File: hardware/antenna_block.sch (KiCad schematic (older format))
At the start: 33 parts, among them P301 BNC

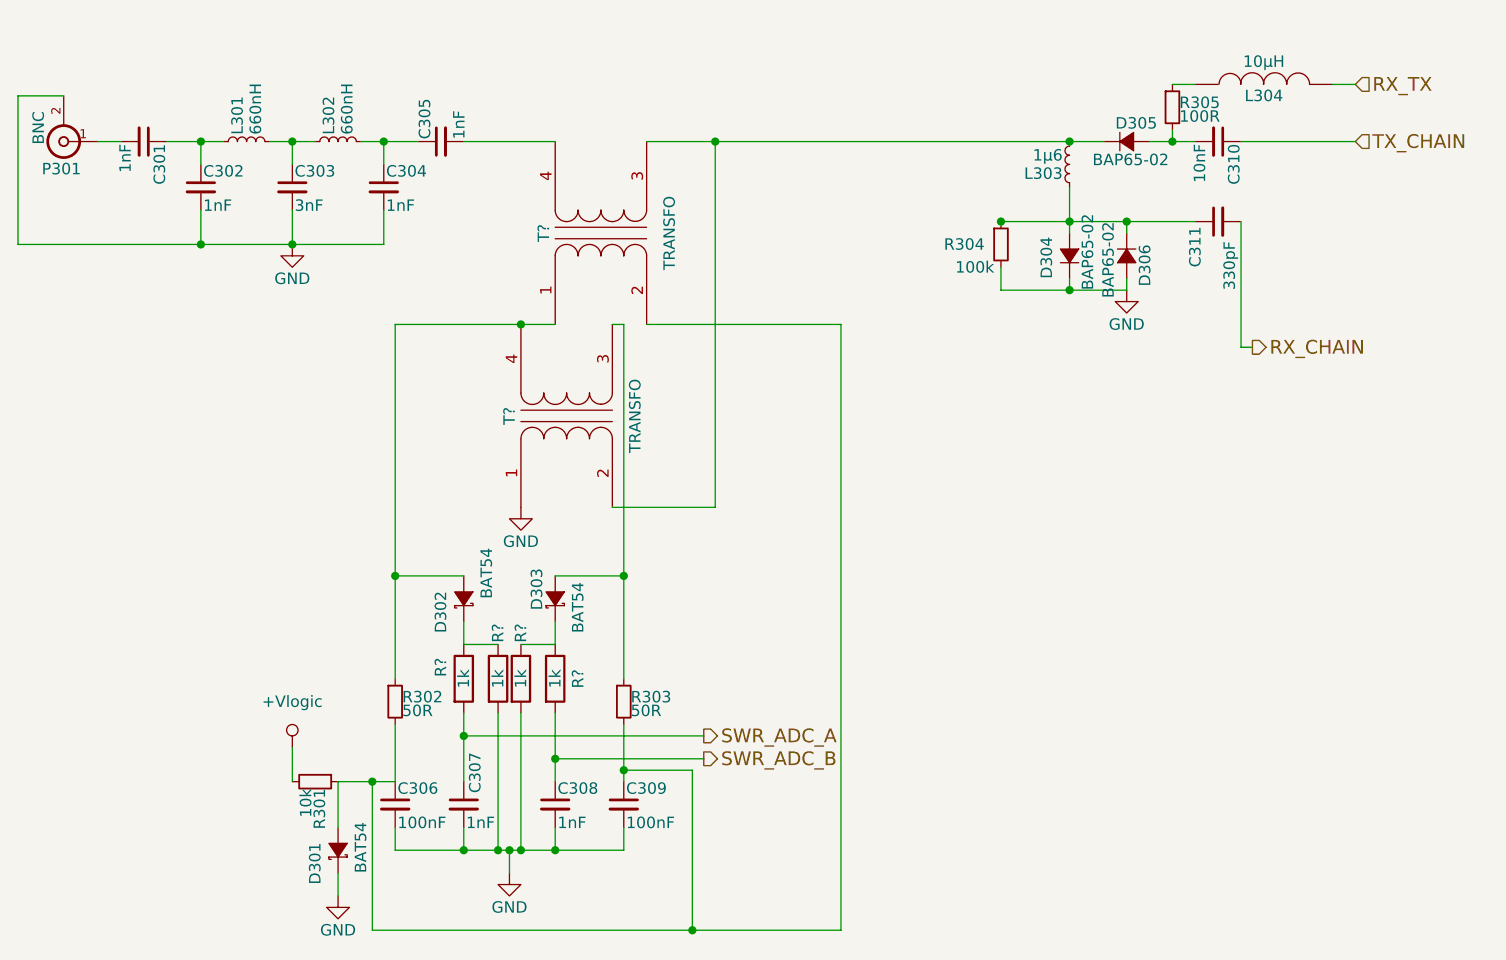
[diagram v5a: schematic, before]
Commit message: Fixed some bugs and annotated rest of the footprints
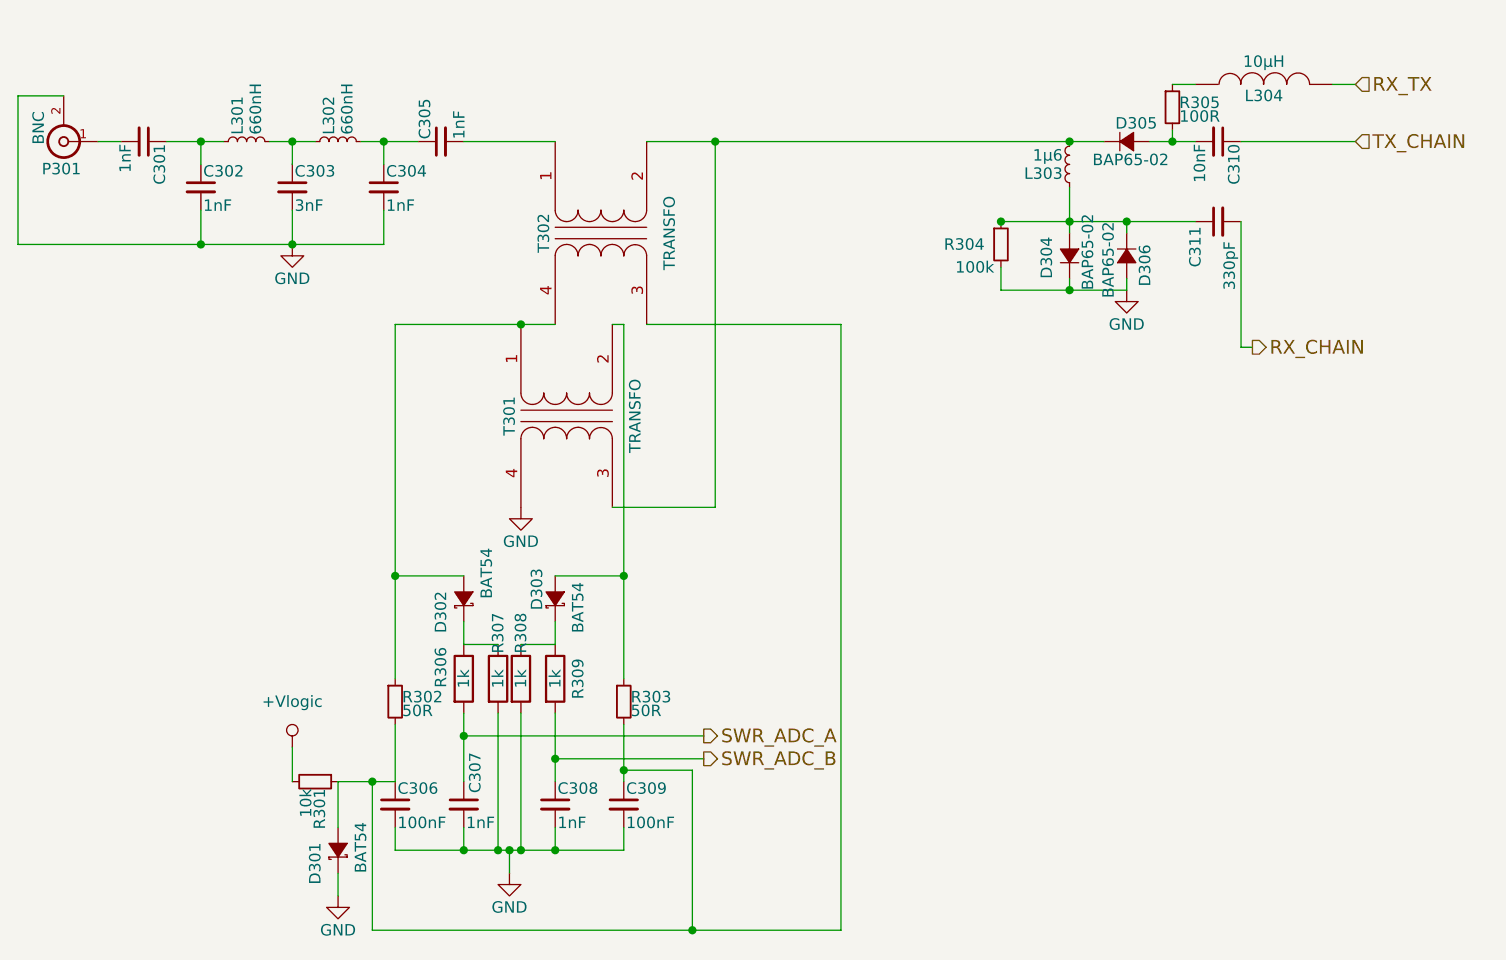
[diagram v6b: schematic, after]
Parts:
- C301, C302, C303, C304, C305, C306, C307, C308, C309, C310, C311: footprint Capacitors_SMD:C_0805 -> Capacitors_SMD:C_0805_HandSoldering
- D304, D305, D306: footprint (none) -> Diodes_SMD:SOD-523
- L301, L302, L303: footprint (none) -> Air_Coils_SML_NEOSID:Neosid_Air-Coil_SML_5turn_HDM0531A
- L304: footprint (none) -> Resistors_SMD:R_0805_HandSoldering
- P301: footprint (none) -> dodekaedri:BNC_right_angle
- R306, R307, R308, R309: renamed from R?; footprint (none) -> Resistors_SMD:R_0805_HandSoldering
- T301, T302: renamed from T?; footprint (none) -> dodekaedri:TRANSF_pads
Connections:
- net GND: now also T301.4 (SB); no longer T301.1 (AA)
- net at C305.2: now also T302.1 (AA); no longer T302.4 (SB)
- net at D302.2 (A), R302.1: now also T301.1 (AA), T302.4 (SB); no longer T301.4 (SB), T302.1 (AA)
- net at C306.1, C309.1, D301.2 (A)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: now also T302.3 (SA); no longer T302.2 (AB)
- net at D303.2 (A), R303.1: now also T301.2 (AB); no longer T301.3 (SA)
- net at D305.1 (K), L303.2: now also T301.3 (SA), T302.2 (AB); no longer T301.2 (AB), T302.3 (SA)
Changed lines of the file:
@@
 F 0 "P301" H 2810 3220 50  0000 C CNN
 F 1 "BNC" V 2910 3040 50  0000 C CNN
-F 2 "" H 2800 3100 50  0001 C CNN
+F 2 "dodekaedri:BNC_right_angle" H 2800 3100 50  0001 C CNN
 F 3 "" H 2800 3100 50  0000 C CNN
 	1    2800 3100
@@
 F 0 "C301" H 3160 3170 50  0000 L CNN
 F 1 "1nF" H 3160 3020 50  0000 L CNN
-F 2 "Capacitors_SMD:C_0805" H 3150 3100 50  0001 C CNN
+F 2 "Capacitors_SMD:C_0805_HandSoldering" H 3150 3100 50  0001 C CNN
 F 3 "" H 3150 3100 50  0000 C CNN
 	1    3150 3100
@@
 F 0 "C302" H 3410 3370 50  0000 L CNN
 F 1 "1nF" H 3410 3220 50  0000 L CNN
-F 2 "Capacitors_SMD:C_0805" H 3400 3300 50  0001 C CNN
+F 2 "Capacitors_SMD:C_0805_HandSoldering" H 3400 3300 50  0001 C CNN
 F 3 "" H 3400 3300 50  0000 C CNN
 	1    3400 3300
@@
 $EndComp
 $Comp
-L GND #PWR301
+L GND #PWR012
 U 1 1 57E329F5
 P 3800 3550
-F 0 "#PWR301" H 3800 3300 50  0001 C CNN
+F 0 "#PWR012" H 3800 3300 50  0001 C CNN
 F 1 "GND" H 3800 3400 50  0000 C CNN
 F 2 "" H 3800 3550 50  0000 C CNN
@@
 F 0 "L301" H 3630 3140 50  0000 L CNN
 F 1 "660nH" H 3630 3060 50  0000 L CNN
-F 2 "" H 3600 3100 50  0001 C CNN
+F 2 "Air_Coils_SML_NEOSID:Neosid_Air-Coil_SML_5turn_HDM0531A" H 3600 3100 50  0001 C CNN
 F 3 "" H 3600 3100 50  0000 C CNN
 	1    3600 3100
@@
 F 0 "L302" H 4030 3140 50  0000 L CNN
 F 1 "660nH" H 4030 3060 50  0000 L CNN
-F 2 "" H 4000 3100 50  0001 C CNN
+F 2 "Air_Coils_SML_NEOSID:Neosid_Air-Coil_SML_5turn_HDM0531A" H 4000 3100 50  0001 C CNN
 F 3 "" H 4000 3100 50  0000 C CNN
 	1    4000 3100
@@
 F 0 "C303" H 3810 3370 50  0000 L CNN
 F 1 "3nF" H 3810 3220 50  0000 L CNN
-F 2 "Capacitors_SMD:C_0805" H 3800 3300 50  0001 C CNN
+F 2 "Capacitors_SMD:C_0805_HandSoldering" H 3800 3300 50  0001 C CNN
 F 3 "" H 3800 3300 50  0000 C CNN
 	1    3800 3300
@@
 F 0 "C304" H 4210 3370 50  0000 L CNN
 F 1 "1nF" H 4210 3220 50  0000 L CNN
-F 2 "Capacitors_SMD:C_0805" H 4200 3300 50  0001 C CNN
+F 2 "Capacitors_SMD:C_0805_HandSoldering" H 4200 3300 50  0001 C CNN
 F 3 "" H 4200 3300 50  0000 C CNN
 	1    4200 3300
@@
 F 0 "C305" H 4460 3170 50  0000 L CNN
 F 1 "1nF" H 4460 3020 50  0000 L CNN
-F 2 "Capacitors_SMD:C_0805" H 4450 3100 50  0001 C CNN
+F 2 "Capacitors_SMD:C_0805_HandSoldering" H 4450 3100 50  0001 C CNN
 F 3 "" H 4450 3100 50  0000 C CNN
 	1    4450 3100
@@
 F 0 "C307" V 4600 6050 50  0000 L CNN
 F 1 "1nF" H 4560 5920 50  0000 L CNN
-F 2 "Capacitors_SMD:C_0805" H 4550 6000 50  0001 C CNN
+F 2 "Capacitors_SMD:C_0805_HandSoldering" H 4550 6000 50  0001 C CNN
 F 3 "" H 4550 6000 50  0000 C CNN
 	1    4550 6000
@@
 F 0 "C308" H 4960 6070 50  0000 L CNN
 F 1 "1nF" H 4960 5920 50  0000 L CNN
-F 2 "Capacitors_SMD:C_0805" H 4950 6000 50  0001 C CNN
+F 2 "Capacitors_SMD:C_0805_HandSoldering" H 4950 6000 50  0001 C CNN
 F 3 "" H 4950 6000 50  0000 C CNN
 	1    4950 6000
@@
 F 0 "C309" H 5260 6070 50  0000 L CNN
 F 1 "100nF" H 5260 5920 50  0000 L CNN
-F 2 "Capacitors_SMD:C_0805" H 5250 6000 50  0001 C CNN
+F 2 "Capacitors_SMD:C_0805_HandSoldering" H 5250 6000 50  0001 C CNN
 F 3 "" H 5250 6000 50  0000 C CNN
 	1    5250 6000
@@
 F 0 "C306" H 4260 6070 50  0000 L CNN
 F 1 "100nF" H 4260 5920 50  0000 L CNN
-F 2 "Capacitors_SMD:C_0805" H 4250 6000 50  0001 C CNN
+F 2 "Capacitors_SMD:C_0805_HandSoldering" H 4250 6000 50  0001 C CNN
 F 3 "" H 4250 6000 50  0000 C CNN
 	1    4250 6000
@@
 $EndComp
 $Comp
-L +Vlogic #PWR302
+L +Vlogic #PWR013
 U 1 1 57E32A6B
 P 3800 5750
-F 0 "#PWR302" H 3800 5550 50  0001 C CNN
+F 0 "#PWR013" H 3800 5550 50  0001 C CNN
 F 1 "+Vlogic" H 3800 5950 50  0000 C CNN
 F 2 "" H 3800 5750 50  0000 C CNN
@@
 $EndComp
 $Comp
-L GND #PWR304
+L GND #PWR014
 U 1 1 57E32A71
 P 4750 6300
-F 0 "#PWR304" H 4750 6050 50  0001 C CNN
+F 0 "#PWR014" H 4750 6050 50  0001 C CNN
 F 1 "GND" H 4750 6150 50  0000 C CNN
 F 2 "" H 4750 6300 50  0000 C CNN
@@
 Connection ~ 4950 5800
 $Comp
-L GND #PWR303
+L GND #PWR015
 U 1 1 57E32AAA
 P 4000 6400
-F 0 "#PWR303" H 4000 6150 50  0001 C CNN
+F 0 "#PWR015" H 4000 6150 50  0001 C CNN
 F 1 "GND" H 4000 6250 50  0000 C CNN
 F 2 "" H 4000 6400 50  0000 C CNN
@@
 F 0 "L303" H 7230 3240 50  0000 L CNN
 F 1 "1µ6" H 7230 3160 50  0000 L CNN
-F 2 "" H 7200 3200 50  0001 C CNN
+F 2 "Air_Coils_SML_NEOSID:Neosid_Air-Coil_SML_5turn_HDM0531A" H 7200 3200 50  0001 C CNN
 F 3 "" H 7200 3200 50  0000 C CNN
 	1    7200 3200
@@
 F 0 "D304" H 7100 3700 50  0000 L CNN
 F 1 "BAP65-02" H 7050 3520 50  0000 L CNN
-F 2 "" V 7200 3600 50  0001 C CNN
+F 2 "Diodes_SMD:SOD-523" V 7200 3600 50  0001 C CNN
 F 3 "" V 7200 3600 50  0000 C CNN
 	1    7200 3600
@@
 F 0 "C311" H 7650 3550 50  0000 L CNN
 F 1 "330pF" H 7550 3400 50  0000 L CNN
-F 2 "Capacitors_SMD:C_0805" H 7850 3450 50  0001 C CNN
+F 2 "Capacitors_SMD:C_0805_HandSoldering" H 7850 3450 50  0001 C CNN
 F 3 "" H 7850 3450 50  0000 C CNN
 	1    7850 3450
@@
 F 0 "D305" H 7400 3180 50  0000 L CNN
 F 1 "BAP65-02" H 7300 3020 50  0000 L CNN
-F 2 "" V 7450 3100 50  0001 C CNN
+F 2 "Diodes_SMD:SOD-523" V 7450 3100 50  0001 C CNN
 F 3 "" V 7450 3100 50  0000 C CNN
 	1    7450 3100
@@
 F 0 "C310" H 7860 3170 50  0000 L CNN
 F 1 "10nF" H 7860 3020 50  0000 L CNN
-F 2 "Capacitors_SMD:C_0805" H 7850 3100 50  0001 C CNN
+F 2 "Capacitors_SMD:C_0805_HandSoldering" H 7850 3100 50  0001 C CNN
 F 3 "" H 7850 3100 50  0000 C CNN
 	1    7850 3100
@@
 Connection ~ 6900 3450
 $Comp
-L GND #PWR305
+L GND #PWR016
 U 1 1 57E32AFA
 P 7450 3750
-F 0 "#PWR305" H 7450 3500 50  0001 C CNN
+F 0 "#PWR016" H 7450 3500 50  0001 C CNN
 F 1 "GND" H 7450 3600 50  0000 C CNN
 F 2 "" H 7450 3750 50  0000 C CNN
@@
 F 0 "L304" V 8000 2850 50  0000 C CNN
 F 1 "10µH" V 8150 2850 50  0000 C CNN
-F 2 "" H 8050 2850 50  0001 C CNN
+F 2 "Resistors_SMD:R_0805_HandSoldering" H 8050 2850 50  0001 C CNN
 F 3 "" H 8050 2850 50  0000 C CNN
 	1    8050 2850
@@
 F 0 "D306" H 7400 3680 50  0000 L CNN
 F 1 "BAP65-02" H 7300 3520 50  0000 L CNN
-F 2 "" V 7450 3600 50  0001 C CNN
+F 2 "Diodes_SMD:SOD-523" V 7450 3600 50  0001 C CNN
 F 3 "" V 7450 3600 50  0000 C CNN
 	1    7450 3600
@@
 Connection ~ 7450 3450
 $Comp
-L TRANSFO T?
+L TRANSFO T302
 U 1 1 57F12697
 P 5150 3500
-F 0 "T?" H 5150 3750 50  0000 C CNN
+F 0 "T302" H 5150 3750 50  0000 C CNN
 F 1 "TRANSFO" H 5150 3200 50  0000 C CNN
-F 2 "" H 5150 3500 50  0000 C CNN
+F 2 "dodekaedri:TRANSF_pads" H 5150 3500 50  0001 C CNN
 F 3 "" H 5150 3500 50  0000 C CNN
 	1    5150 3500
-	0    -1   -1   0
-$EndComp
-$Comp
-L TRANSFO T?
+	0    -1   1    0
+$EndComp
+$Comp
+L TRANSFO T301
 U 1 1 57F12E63
 P 5000 4300
-F 0 "T?" H 5000 4550 50  0000 C CNN
+F 0 "T301" H 5000 4550 50  0000 C CNN
 F 1 "TRANSFO" H 5000 4000 50  0000 C CNN
-F 2 "" H 5000 4300 50  0000 C CNN
+F 2 "dodekaedri:TRANSF_pads" H 5000 4300 50  0001 C CNN
 F 3 "" H 5000 4300 50  0000 C CNN
 	1    5000 4300
-	0    -1   -1   0
-$EndComp
-$Comp
-L GND #PWR?
+	0    -1   1    0
+$EndComp
+$Comp
+L GND #PWR017
 U 1 1 57F12F7B
 P 4800 4700
-F 0 "#PWR?" H 4800 4450 50  0001 C CNN
+F 0 "#PWR017" H 4800 4450 50  0001 C CNN
 F 1 "GND" H 4800 4550 50  0000 C CNN
 F 2 "" H 4800 4700 50  0000 C CNN
@@
 Connection ~ 4800 3900
 $Comp
-L R R?
+L R R307
 U 1 1 57F13FE3
 P 4700 5450
-F 0 "R?" V 4700 5650 50  0000 C CNN
+F 0 "R307" V 4700 5650 50  0000 C CNN
 F 1 "1k" V 4700 5450 50  0000 C CNN
-F 2 "" V 4630 5450 50  0000 C CNN
+F 2 "Resistors_SMD:R_0805_HandSoldering" V 4630 5450 50  0001 C CNN
 F 3 "" H 4700 5450 50  0000 C CNN
 	1    4700 5450
@@
 $EndComp
 $Comp
-L R R?
+L R R306
 U 1 1 57F140DF
 P 4550 5450
-F 0 "R?" V 4450 5500 50  0000 C CNN
+F 0 "R306" V 4450 5500 50  0000 C CNN
 F 1 "1k" V 4550 5450 50  0000 C CNN
-F 2 "" V 4480 5450 50  0000 C CNN
+F 2 "Resistors_SMD:R_0805_HandSoldering" V 4480 5450 50  0001 C CNN
 F 3 "" H 4550 5450 50  0000 C CNN
 	1    4550 5450
@@
 $EndComp
 $Comp
-L R R?
+L R R308
 U 1 1 57F14156
 P 4800 5450
-F 0 "R?" V 4800 5650 50  0000 C CNN
+F 0 "R308" V 4800 5650 50  0000 C CNN
 F 1 "1k" V 4800 5450 50  0000 C CNN
-F 2 "" V 4730 5450 50  0000 C CNN
+F 2 "Resistors_SMD:R_0805_HandSoldering" V 4730 5450 50  0001 C CNN
 F 3 "" H 4800 5450 50  0000 C CNN
 	1    4800 5450
@@
 $EndComp
 $Comp
-L R R?
+L R R309
 U 1 1 57F141F4
 P 4950 5450
-F 0 "R?" V 5050 5450 50  0000 C CNN
+F 0 "R309" V 5050 5450 50  0000 C CNN
 F 1 "1k" V 4950 5450 50  0000 C CNN
-F 2 "" V 4880 5450 50  0000 C CNN
+F 2 "Resistors_SMD:R_0805_HandSoldering" V 4880 5450 50  0001 C CNN
 F 3 "" H 4950 5450 50  0000 C CNN
 	1    4950 5450

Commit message: halfway through layout
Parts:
- removed C303: 3nF, Capacitors_SMD:C_0805_HandSoldering, symbol C_Small
- removed L302: 660nH, Air_Coils_SML_NEOSID:Neosid_Air-Coil_SML_5turn_HDM0531A, symbol L_Small
- D301, D302, D303: footprint TO_SOT_Packages_SMD:SOT-23_Handsoldering -> dodekaedri:SOT-23_HS_2-1-3
- L304: value 10µH -> 470µH; footprint Resistors_SMD:R_0805_HandSoldering -> dodekaedri:SMT_1007
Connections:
- net at L301.2: now also C304.1, C305.1
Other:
- moved on the sheet: C301, C302, L301, P301
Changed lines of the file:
@@
 L BNC P301
 U 1 1 57E329E0
-P 2800 3100
-F 0 "P301" H 2810 3220 50  0000 C CNN
-F 1 "BNC" V 2910 3040 50  0000 C CNN
-F 2 "dodekaedri:BNC_right_angle" H 2800 3100 50  0001 C CNN
-F 3 "" H 2800 3100 50  0000 C CNN
-	1    2800 3100
+P 3200 3100
+F 0 "P301" H 3210 3220 50  0000 C CNN
+F 1 "BNC" V 3310 3040 50  0000 C CNN
+F 2 "dodekaedri:BNC_right_angle" H 3200 3100 50  0001 C CNN
+F 3 "" H 3200 3100 50  0000 C CNN
+	1    3200 3100
 	-1   0    0    1
 $EndComp
@@
 L C_Small C301
 U 1 1 57E329E7
-P 3150 3100
-F 0 "C301" H 3160 3170 50  0000 L CNN
-F 1 "1nF" H 3160 3020 50  0000 L CNN
-F 2 "Capacitors_SMD:C_0805_HandSoldering" H 3150 3100 50  0001 C CNN
-F 3 "" H 3150 3100 50  0000 C CNN
-	1    3150 3100
+P 3550 3100
+F 0 "C301" H 3560 3170 50  0000 L CNN
+F 1 "1nF" H 3560 3020 50  0000 L CNN
+F 2 "Capacitors_SMD:C_0805_HandSoldering" H 3550 3100 50  0001 C CNN
+F 3 "" H 3550 3100 50  0000 C CNN
+	1    3550 3100
 	0    1    1    0
 $EndComp
@@
 L C_Small C302
 U 1 1 57E329EE
-P 3400 3300
-F 0 "C302" H 3410 3370 50  0000 L CNN
-F 1 "1nF" H 3410 3220 50  0000 L CNN
-F 2 "Capacitors_SMD:C_0805_HandSoldering" H 3400 3300 50  0001 C CNN
-F 3 "" H 3400 3300 50  0000 C CNN
-	1    3400 3300
+P 3800 3300
+F 0 "C302" H 3810 3370 50  0000 L CNN
+F 1 "1nF" H 3810 3220 50  0000 L CNN
+F 2 "Capacitors_SMD:C_0805_HandSoldering" H 3800 3300 50  0001 C CNN
+F 3 "" H 3800 3300 50  0000 C CNN
+	1    3800 3300
 	1    0    0    -1
 $EndComp
@@
 L L_Small L301
 U 1 1 57E329FB
-P 3600 3100
-F 0 "L301" H 3630 3140 50  0000 L CNN
-F 1 "660nH" H 3630 3060 50  0000 L CNN
-F 2 "Air_Coils_SML_NEOSID:Neosid_Air-Coil_SML_5turn_HDM0531A" H 3600 3100 50  0001 C CNN
-F 3 "" H 3600 3100 50  0000 C CNN
-	1    3600 3100
-	0    -1   -1   0
-$EndComp
-$Comp
-L L_Small L302
-U 1 1 57E32A02
 P 4000 3100
-F 0 "L302" H 4030 3140 50  0000 L CNN
+F 0 "L301" H 4030 3140 50  0000 L CNN
 F 1 "660nH" H 4030 3060 50  0000 L CNN
 F 2 "Air_Coils_SML_NEOSID:Neosid_Air-Coil_SML_5turn_HDM0531A" H 4000 3100 50  0001 C CNN
@@
 	1    4000 3100
 	0    -1   -1   0
-$EndComp
-$Comp
-L C_Small C303
-U 1 1 57E32A09
-P 3800 3300
-F 0 "C303" H 3810 3370 50  0000 L CNN
-F 1 "3nF" H 3810 3220 50  0000 L CNN
-F 2 "Capacitors_SMD:C_0805_HandSoldering" H 3800 3300 50  0001 C CNN
-F 3 "" H 3800 3300 50  0000 C CNN
-	1    3800 3300
-	1    0    0    -1
 $EndComp
 $Comp
@@
 F 0 "D301" H 3850 6300 50  0000 L CNN
 F 1 "BAT54" H 3900 6100 50  0000 L CNN
-F 2 "TO_SOT_Packages_SMD:SOT-23_Handsoldering" V 4000 6200 50  0001 C CNN
+F 2 "dodekaedri:SOT-23_HS_2-1-3" V 4000 6200 50  0001 C CNN
 F 3 "" V 4000 6200 50  0000 C CNN
 	1    4000 6200
@@
 F 0 "D302" H 4400 5200 50  0000 L CNN
 F 1 "BAT54" H 4550 5000 50  0000 L CNN
-F 2 "TO_SOT_Packages_SMD:SOT-23_Handsoldering" V 4550 5100 50  0001 C CNN
+F 2 "dodekaedri:SOT-23_HS_2-1-3" V 4550 5100 50  0001 C CNN
 F 3 "" V 4550 5100 50  0000 C CNN
 	1    4550 5100
@@
 F 0 "D303" H 4900 5180 50  0000 L CNN
 F 1 "BAT54" H 4800 5000 50  0000 L CNN
-F 2 "TO_SOT_Packages_SMD:SOT-23_Handsoldering" V 4950 5100 50  0001 C CNN
+F 2 "dodekaedri:SOT-23_HS_2-1-3" V 4950 5100 50  0001 C CNN
 F 3 "" V 4950 5100 50  0000 C CNN
 	1    4950 5100
@@
 $EndComp
 Wire Wire Line
-	2950 3100 3050 3100
-Wire Wire Line
-	3250 3100 3500 3100
-Wire Wire Line
-	3400 3100 3400 3200
-Connection ~ 3400 3100
-Wire Wire Line
-	3700 3100 3900 3100
-Wire Wire Line
-	3800 3200 3800 3100
+	3350 3100 3450 3100
+Wire Wire Line
+	3650 3100 3900 3100
+Wire Wire Line
+	3800 3100 3800 3200
 Connection ~ 3800 3100
 Wire Wire Line
-	3400 3400 3400 3550
-Wire Wire Line
-	2600 3550 4200 3550
-Wire Wire Line
-	3800 3550 3800 3400
-Wire Wire Line
-	2800 2900 2600 2900
-Wire Wire Line
-	2600 2900 2600 3550
-Connection ~ 3400 3550
-Wire Wire Line
-	4100 3100 4350 3100
-Wire Wire Line
-	4200 3100 4200 3200
+	3800 3400 3800 3550
+Wire Wire Line
+	3000 3550 4200 3550
+Wire Wire Line
+	3200 2900 3000 2900
+Wire Wire Line
+	3000 2900 3000 3550
+Connection ~ 3800 3550
 Wire Wire Line
 	4200 3550 4200 3400
-Connection ~ 3800 3550
 Connection ~ 4200 3100
 Wire Wire Line
@@
 P 8050 2850
 F 0 "L304" V 8000 2850 50  0000 C CNN
-F 1 "10µH" V 8150 2850 50  0000 C CNN
-F 2 "Resistors_SMD:R_0805_HandSoldering" H 8050 2850 50  0001 C CNN
+F 1 "470µH" V 8150 2850 50  0000 C CNN
+F 2 "dodekaedri:SMT_1007" H 8050 2850 50  0001 C CNN
 F 3 "" H 8050 2850 50  0000 C CNN
 	1    8050 2850
@@
 U 1 1 57F13FE3
 P 4700 5450
-F 0 "R307" V 4700 5650 50  0000 C CNN
+F 0 "R307" V 4700 5700 50  0000 C CNN
 F 1 "1k" V 4700 5450 50  0000 C CNN
 F 2 "Resistors_SMD:R_0805_HandSoldering" V 4630 5450 50  0001 C CNN
@@
 U 1 1 57F14156
 P 4800 5450
-F 0 "R308" V 4800 5650 50  0000 C CNN
+F 0 "R308" V 4800 5700 50  0000 C CNN
 F 1 "1k" V 4800 5450 50  0000 C CNN
 F 2 "Resistors_SMD:R_0805_HandSoldering" V 4730 5450 50  0001 C CNN
@@
 	6200 3900 6200 6550
 Connection ~ 5550 6550
+Wire Wire Line
+	4200 3200 4200 3100
+Wire Wire Line
+	4100 3100 4350 3100
 $EndSCHEMATC
